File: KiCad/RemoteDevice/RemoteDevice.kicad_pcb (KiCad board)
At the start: 2 copper layers, 98 x 52 mm, 56 parts, among them J1 pin, J2 pin, Q1 PJA3411, Q2 PJA3411, SW1 BP, SW2 BP, U1 XC9140, U10 XBEE-3, U2 STM32L041F6Px, U3 MCP6281, U4 ADT7410TRZ, U5 MCP6281, U6 RT606, U7 Microphone, U8 LD2981CU33, U9 Con_4pts

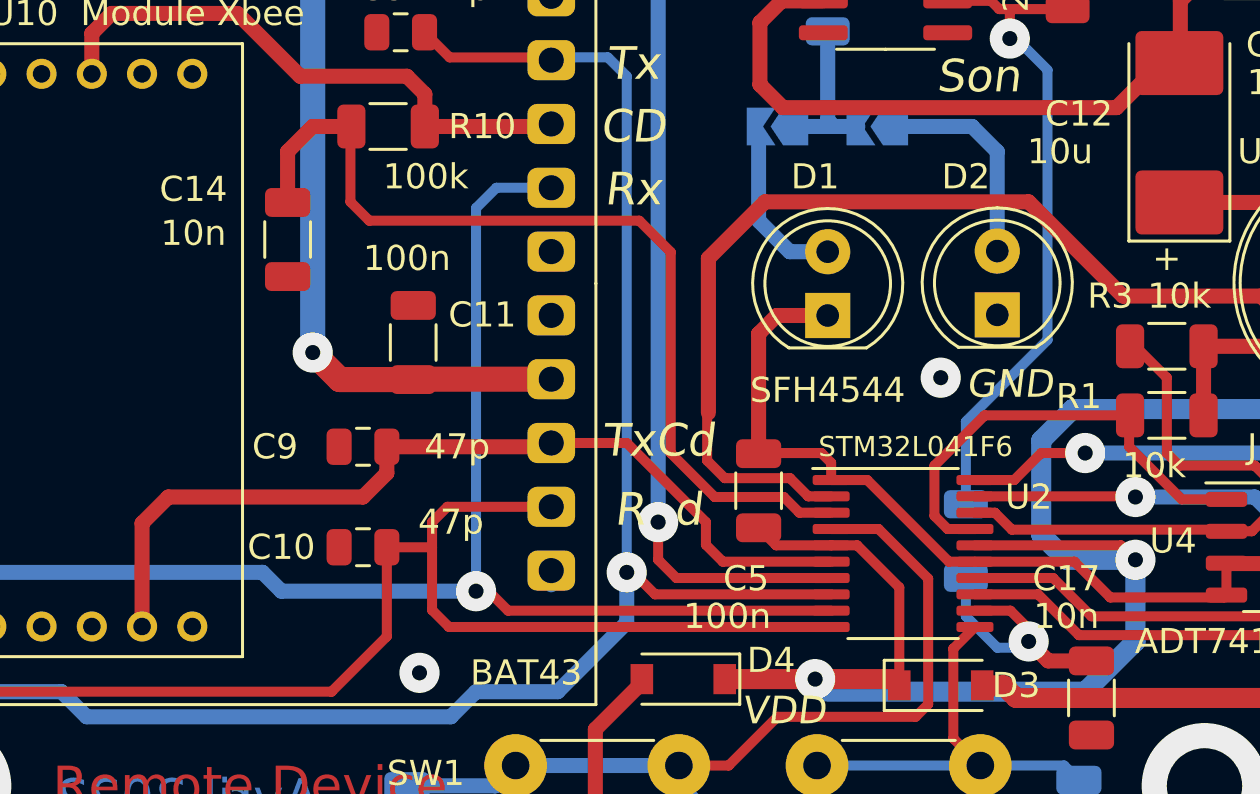
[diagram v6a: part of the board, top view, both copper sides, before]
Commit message: schéma revu avec quelques valeurs retouchées : val correspondent à l'assemblage. Board non mis à jour pour si peu. Le silkscreen est modifié par contre
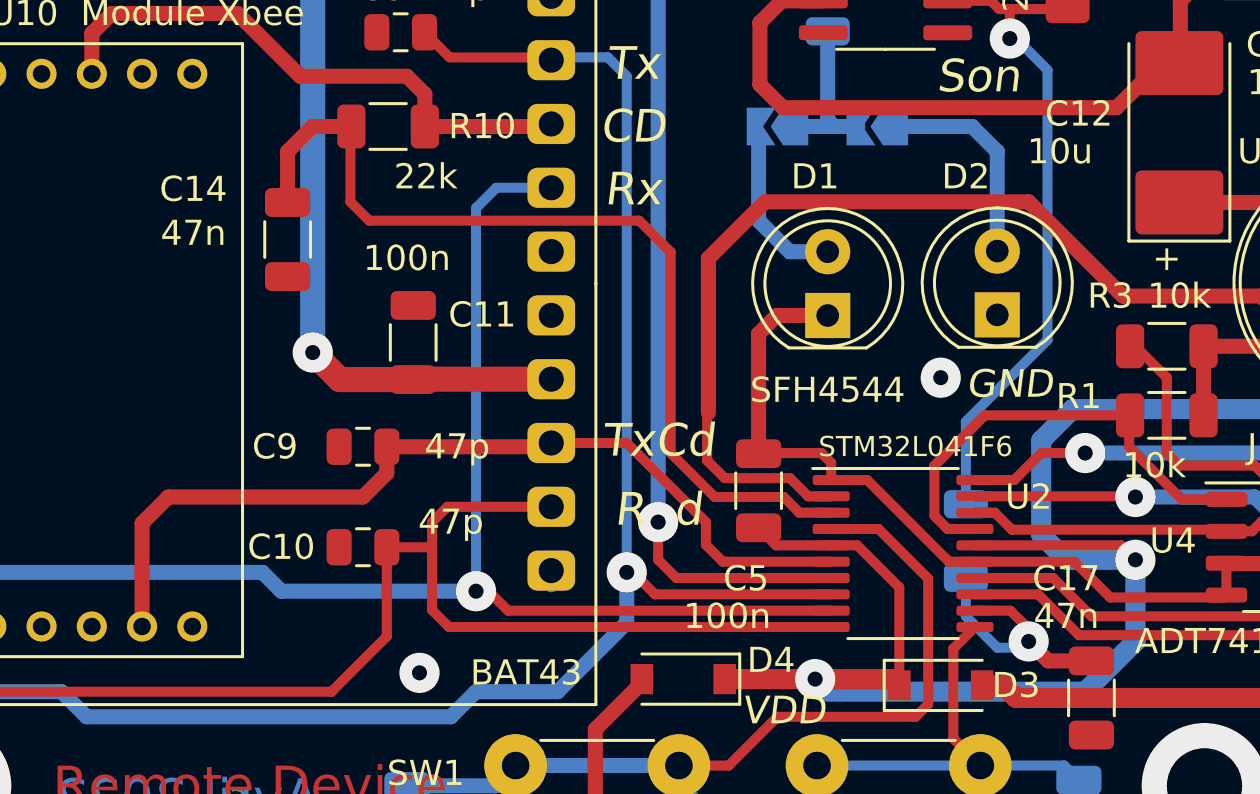
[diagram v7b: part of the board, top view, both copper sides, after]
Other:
- board text added: "150"
- board text added: "22k"
- board text added: "47n"
- board text removed: "100k"
- board text removed: "10n"
- board text removed: "4.7k"
- board text removed: "47"
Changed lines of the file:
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@@
     (effects (font (size 1 1) (thickness 0.15)) (justify mirror))
   )
-  (gr_text "4.7k" (at 76.25 99.75) (layer "B.SilkS")
+  (gr_text "1k" (at 76.25 99.75) (layer "B.SilkS")
     (effects (font (size 1 1) (thickness 0.15)) (justify mirror))
   )
-  (gr_text "47" (at 71.5 76.75) (layer "B.SilkS")
+  (gr_text "150" (at 71.5 76.75) (layer "B.SilkS")
     (effects (font (size 1 1) (thickness 0.15)) (justify mirror))
   )
@@
     (effects (font (size 1 1) (thickness 0.15)))
   )
-  (gr_text "10n\n" (at 83.5 102.25) (layer "F.SilkS")
+  (gr_text "47n" (at 83.5 102.25) (layer "F.SilkS")
     (effects (font (size 1 1) (thickness 0.15)))
   )
@@
     (effects (font (size 1 1) (thickness 0.15)))
   )
-  (gr_text "100k\n" (at 58 84.75) (layer "F.SilkS")
+  (gr_text "22k" (at 58 84.75) (layer "F.SilkS")
     (effects (font (size 1 1) (thickness 0.15)))
   )
@@
     (effects (font (size 1 1) (thickness 0.15)))
   )
-  (gr_text "10n" (at 48.75 87) (layer "F.SilkS")
+  (gr_text "47n" (at 48.75 87) (layer "F.SilkS")
     (effects (font (size 1 1) (thickness 0.15)))
   )

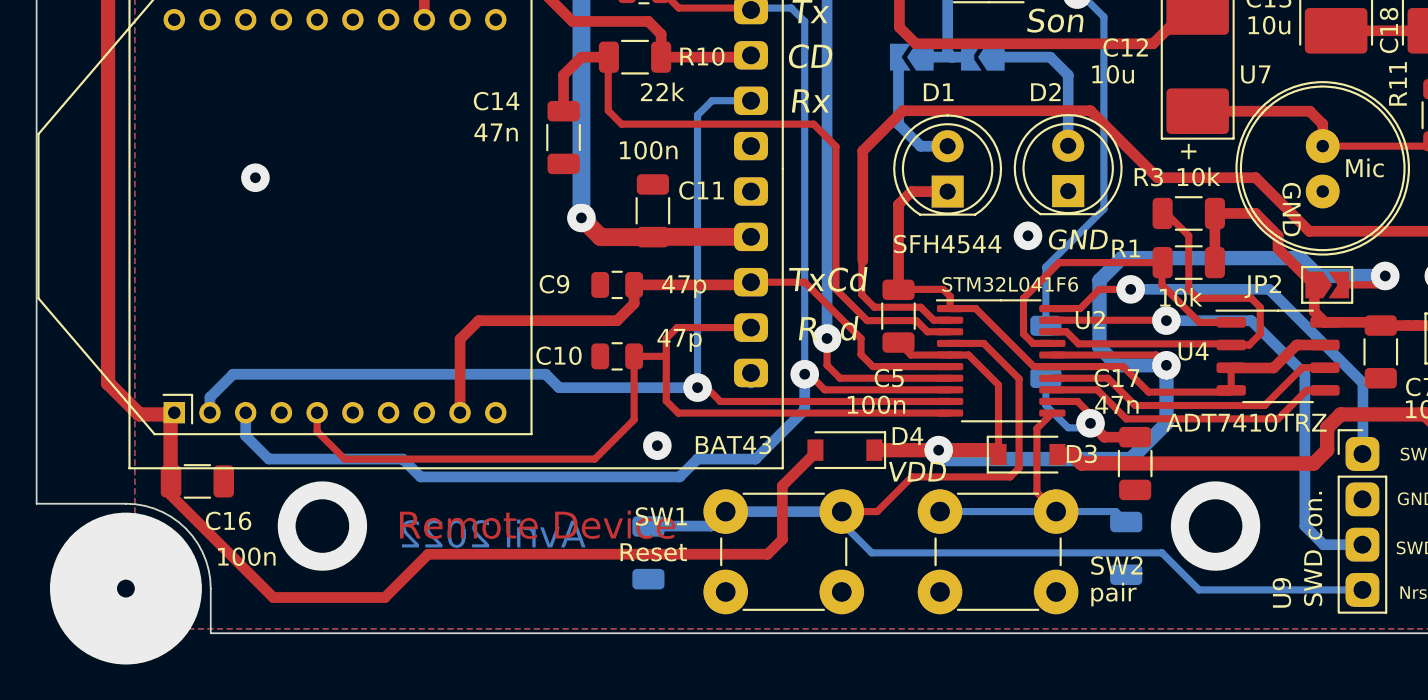
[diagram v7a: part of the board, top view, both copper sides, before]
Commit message: Version modifié : ajout pull up RT606 pour adapt niveau, supression BAT43, ajout capa de découplage uC. A tester
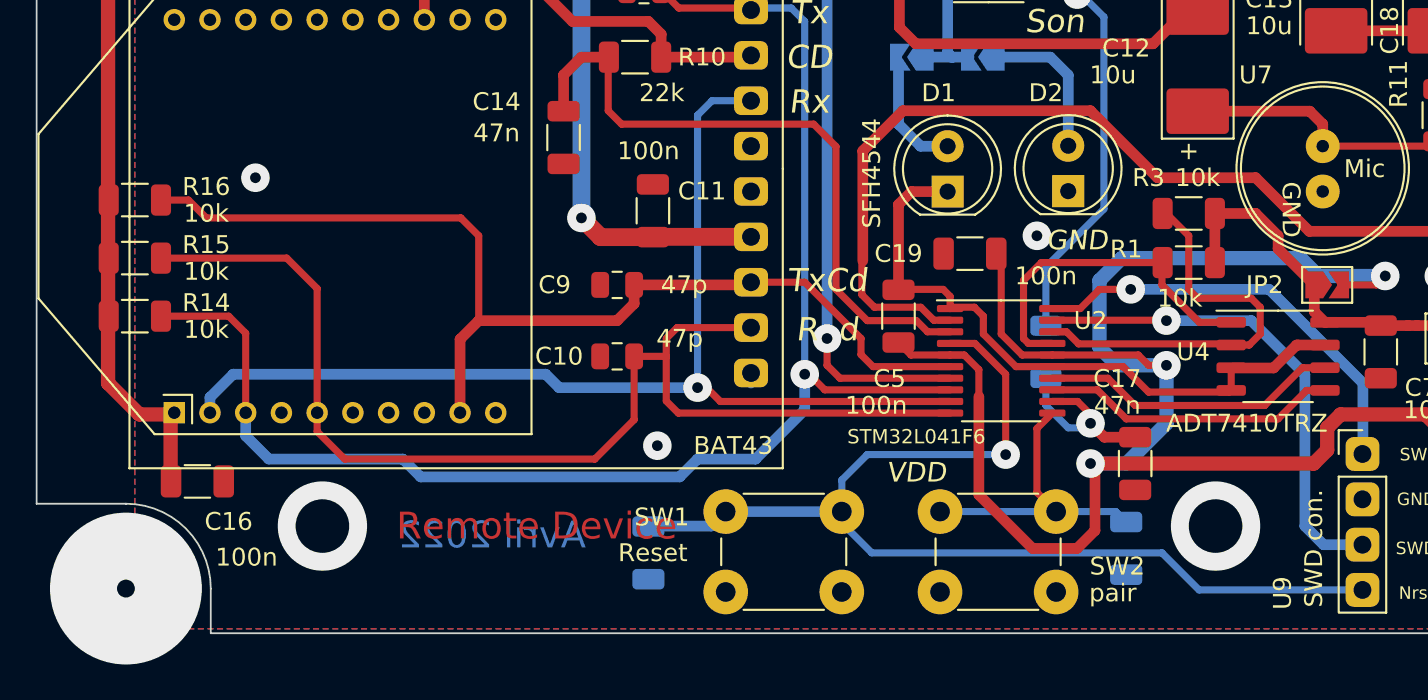
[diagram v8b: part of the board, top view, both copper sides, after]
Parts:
- removed D3, D4: BAT43W-V, Diode_SMD:D_SOD-123
- added C19: 100n, Capacitor_SMD:C_1206_3216Metric, F.Cu at (75.2, 93.8)
- added R14: 10k, Resistor_SMD:R_1206_3216Metric, F.Cu at (28.5, 97.2)
- added R15: 10k, Resistor_SMD:R_1206_3216Metric, F.Cu at (28.5, 94.0)
- added R16: 10k, Resistor_SMD:R_1206_3216Metric, F.Cu at (28.5, 90.8)
- C14, C17: value 10n -> 47n
- R10: value 100k -> 22k
- R12: value 4.7k -> 1k
- R4: value 47 -> 150
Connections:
- C5 pad 1: VDD -> +3V0
- JP2 pad 2: VDD -> +3V0
- U2 pad 16: VDD -> +3V0
- U2 pad 5: VDD -> +3V0
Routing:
- net +3V0: track 101.8 -> 173.6 mm, vias 0 -> 3
- net VDD: track 68.3 -> 0.00 mm, vias 3 -> 0
- net +3V3: track 259.6 -> 215.1 mm
- net /TxCmde: track 36.0 -> 59.3 mm
- net /RxCmde: track 50.4 -> 66.8 mm
- net /DataIn: track 74.2 -> 83.8 mm
- net /Reset: track 63.1 -> 62.4 mm, vias 0 -> 1
- net /SCL: track 18.5 -> 19.2 mm
- net GND: track 62.5 -> 63.2 mm
